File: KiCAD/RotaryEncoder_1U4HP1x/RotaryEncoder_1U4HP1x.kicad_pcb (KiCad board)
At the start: 2 copper layers, 20.3 x 39.6 mm, 4 parts, among them J1 Conn_01x05_Socket

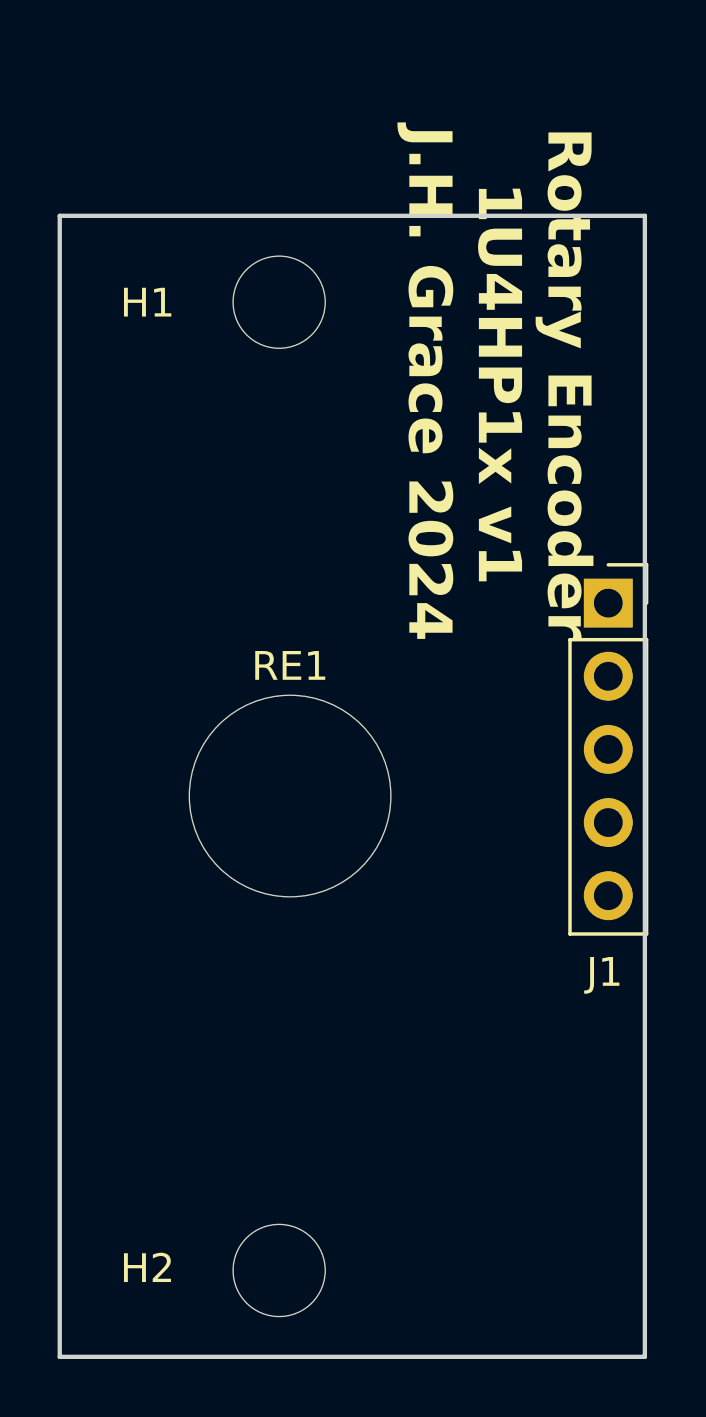
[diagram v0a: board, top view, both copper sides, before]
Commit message: updated PCB widths to better conform to Eurorack standards
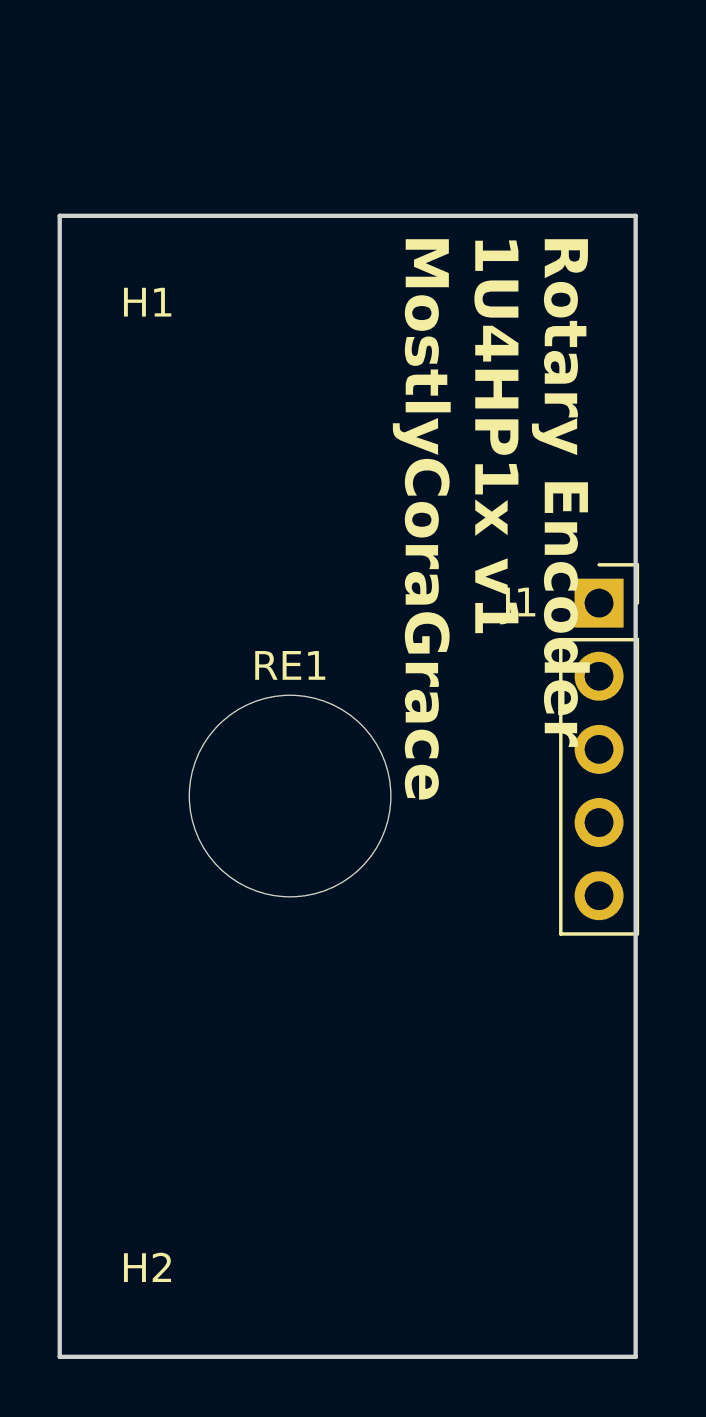
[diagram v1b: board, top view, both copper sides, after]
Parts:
- moved J1 0.32 mm to (18.7, 15.9)
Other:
- board size 20.3 x 39.6 mm -> 20 x 39.6 mm
- board text added: "Rotary Encoder 1U4HP1x v1 MostlyCoraGrace"
- board text removed: "Rotary Encoder 1U4HP1x v1 J.H. Grace 2024"

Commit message: removed all front silkscreen, and flipped most modules, to make the boards 'cleaner'.
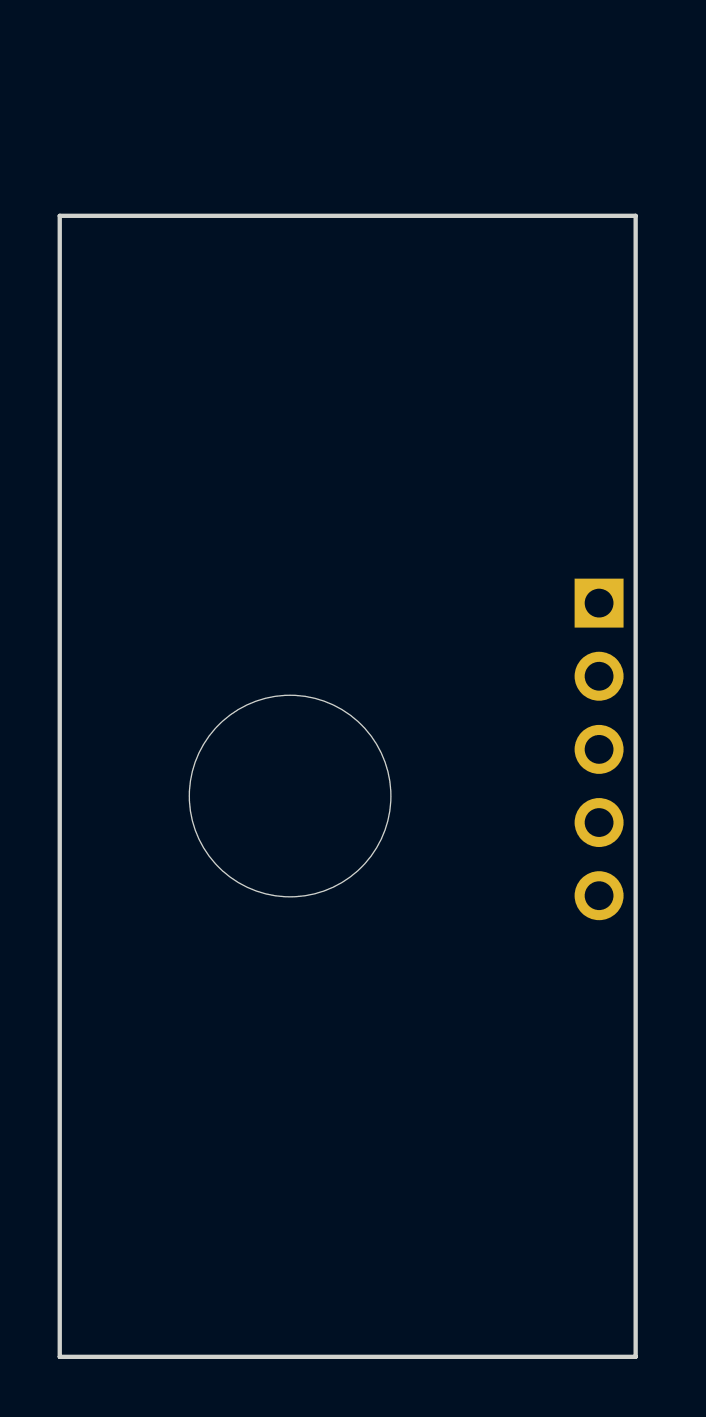
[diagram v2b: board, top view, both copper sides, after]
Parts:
- H1, H2, J1, RE1: moved to B.Cu
- turned H1 to 180 degrees
- turned H2 to 180 degrees
- turned J1 to 180 degrees
- turned RE1 to 180 degrees

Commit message: added copper fills to every module, to maybe possibly increase structural rigidity.
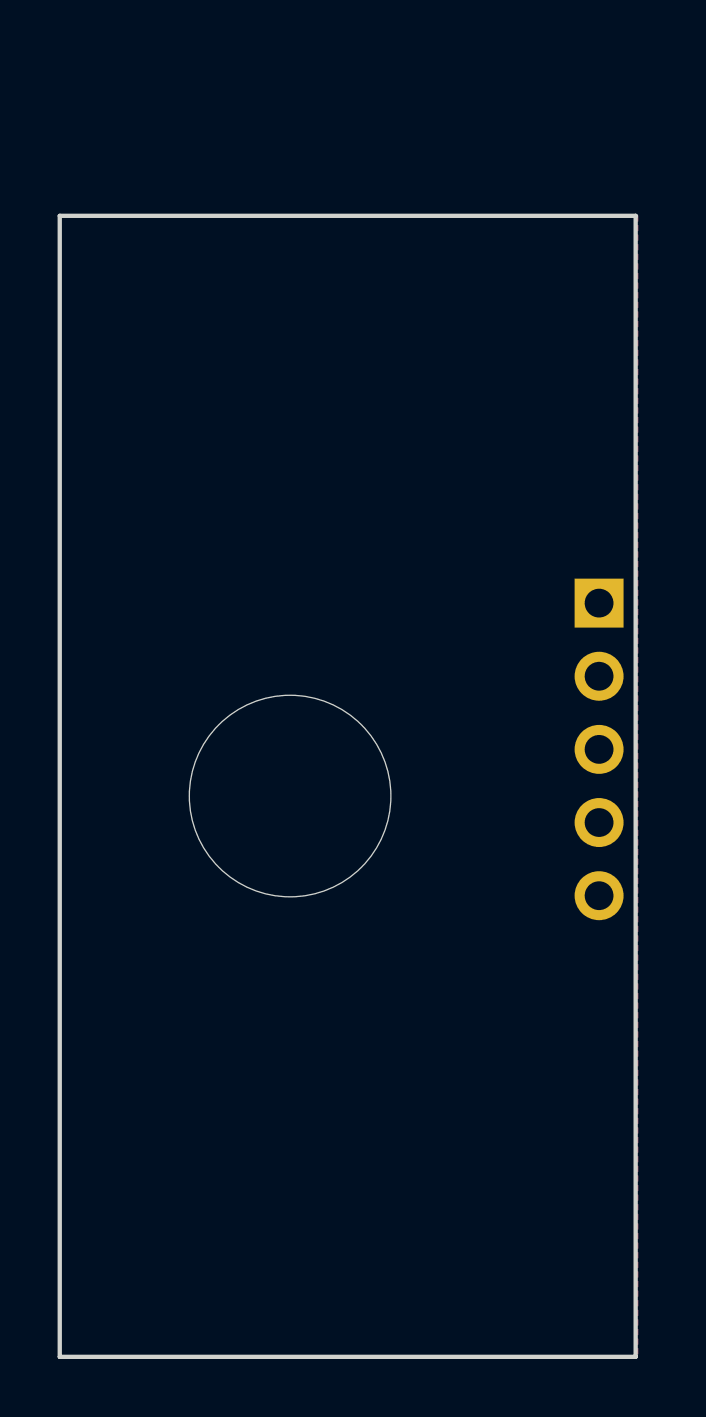
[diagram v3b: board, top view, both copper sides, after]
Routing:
- added copper zone on B.Cu, net (none)
- added copper zone on F.Cu, net (none)
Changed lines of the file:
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@@
+		)
+	)
+	(zone
+		(net 0)
+		(net_name "")
+		(layers "F&B.Cu")
+		(hatch edge 0.5)
+		(connect_pads
+			(clearance 0.5)
+		)
+		(min_thickness 0.25)
+		(filled_areas_thickness no)
+		(fill yes
+			(thermal_gap 0.5)
+			(thermal_bridge_width 0.5)
+			(island_removal_mode 1)
+			(island_area_min 10)
+		)
+		(polygon
+			(pts
+				(xy 0 2.413) (xy 20.066 2.413) (xy 20.066 42.037) (xy 0 42.037)
+			)
 		)
 	)

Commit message: added PCBWay print identification silkscreen text to each component
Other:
- board text added: "WayWayWay"
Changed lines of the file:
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@@
+		)
+	)
+	(gr_text "WayWayWay"
+		(at 1.5 4 90)
+		(layer "B.SilkS")
+		(effects
+			(font
+				(size 1 1)
+				(thickness 0.15)
+			)
+			(justify left top mirror)
 		)
 	)
